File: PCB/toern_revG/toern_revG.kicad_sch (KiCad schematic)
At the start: 106 parts, among them IC1 BQ24075TRGTR, J1 AudioJack3_Switch, J10 Conn_01x02, J11 Conn_01x05, J11.5 Conn_01x05, J12 Conn_01x05, J13 Conn_01x05, J14 Conn_01x05, J15 Conn_01x05, J16 Conn_01x02, J17 AudioJack3_Ground, J18 Conn_01x05_Socket, J19 Conn_01x05_Socket, J2 Conn_01x05_Socket, J20 Conn_01x05_Socket, J21 Conn_01x05_Socket, J22 Conn_01x05_Socket, J23 Conn_01x05_Socket, J24 Conn_01x05_Socket, J3 AudioJack3_Ground, J4 USB_C_Receptacle_USB2.0, J5 AudioJack3_Switch, J6 AudioJack3_Switch, J7 AudioJack3_Switch, J8 Micro_SD_Card, J9 Conn_01x03, U1 SPX3819M5-L-3-3, U10 01x05 Connector_PinSocket_2.5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, U11 01x05 Connector_PinSocket_2.5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, U12 01x05 Connector_PinSocket_2.5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, U13 PAM8403D, U2 SPX3819M5-L-1-8, U3 SGTL5000XNBA3, U4 TLP2361V4_E, U5 74LVC2G14, U6 Teensy4.1, U7 SPX3819M5-L-3-3, U9 01x05 Connector_PinSocket_2.5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

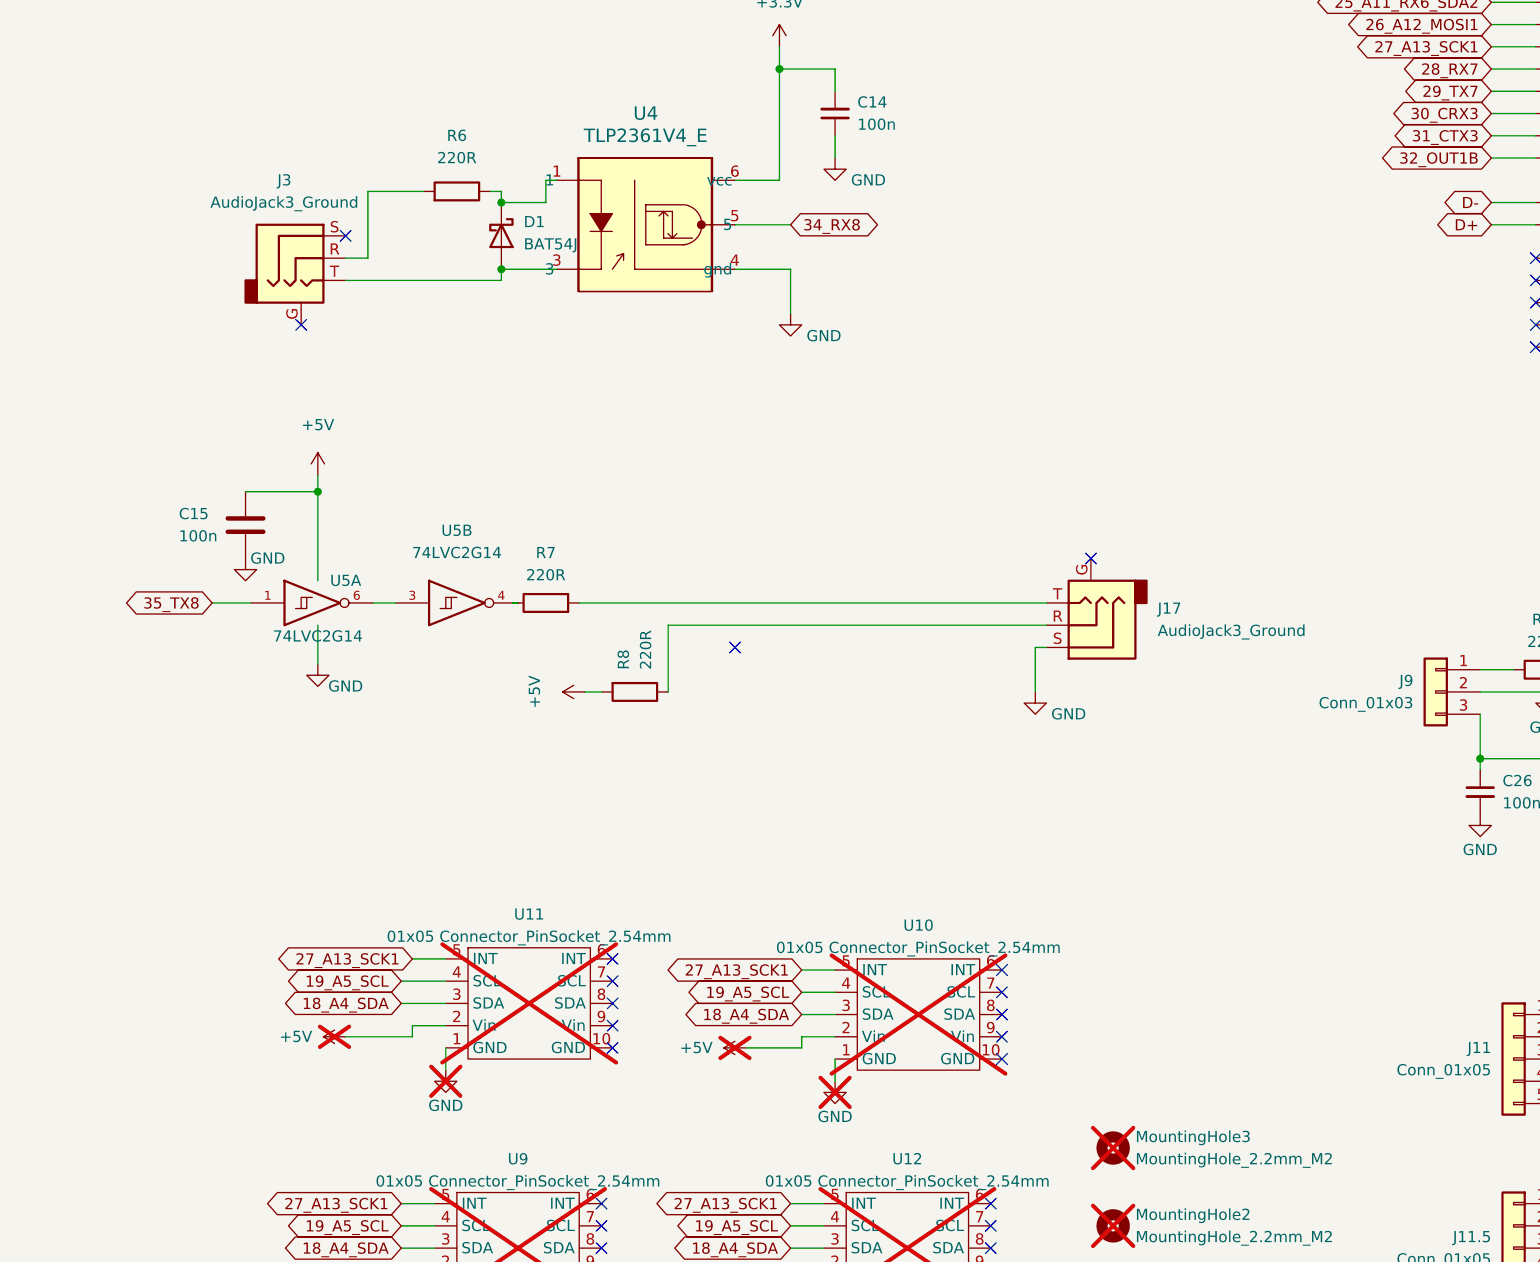
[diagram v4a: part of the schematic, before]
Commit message: better loading and saving speed and progress
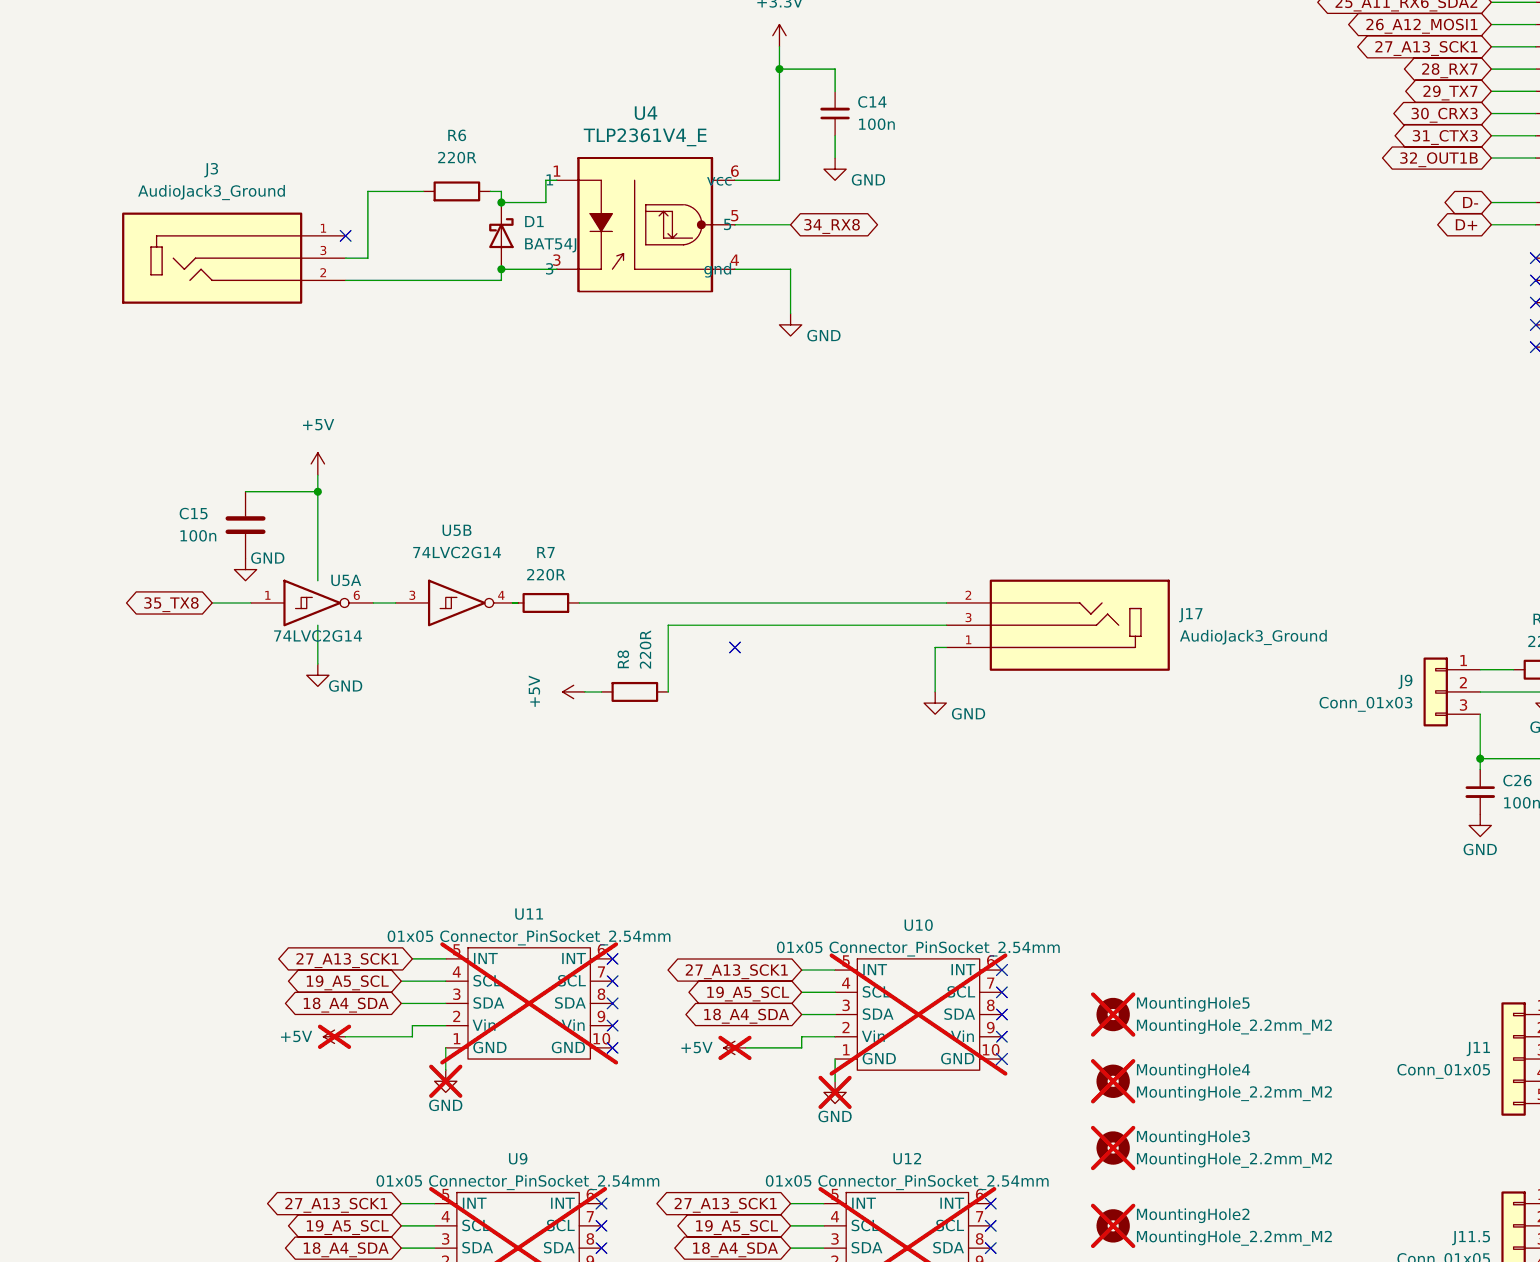
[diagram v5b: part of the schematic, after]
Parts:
- added MountingHole4, MountingHole5: MountingHole_2.2mm_M2, MountingHole:MountingHole_2.2mm_M2, symbol Mechanical:MountingHole
- IC1: footprint QFN50P300X300X100-17N-D -> BQ24075TRGTR:QFN50P300X300X100-17N-D
- J17, J3: footprint Connector_Audio:Jack_3.5mm_CUI_SJ1-3533NG_Horizontal_CircularHoles -> SJ1-3533:CUI_SJ1-3533; symbol Connector_Audio:AudioJack3_Ground -> SJ1-3533:SJ1-3533; Availability (none) -> In Stock; Check_prices (none) -> https://www.snapeda.com/parts/SJ1-3533/Same+Sky/view-part/?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; Description_1 (none) -> 3.5 mm Right-Angle Stereo Jack, 3 Pin PCB Mount, Threaded w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; LCSC C4992548 -> C4991776; MANUFACTURER (none) -> CUI Devices; MF (none) -> Same Sky; MP (none) -> SJ1-3533; PARTREV (none) -> 1.01; Package (none) -> None; Price (none) -> None; STANDARD (none) -> Manufacturer Recommendations; SnapEDA_Link (none) -> https://www.snapeda.com/parts/SJ1-3533/Same+Sky/view-part/?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; lcsc# C4992548 -> C4991776
- S1: footprint Button_Switch_THT:SW_E-Switch_EG2219_DPDT_Angled -> EG2219:EG2219
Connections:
- net GND: now also J17.1; no longer J17.S
- net at R7.2: now also J17.2; no longer J17.T
- net at R6.2: now also J3.3; no longer J3.R
- net at D1.2 (A), U4.3: now also J3.2; no longer J3.T
- net at R8.1: now also J17.3; no longer J17.R
- no-connect marks 64 -> 62

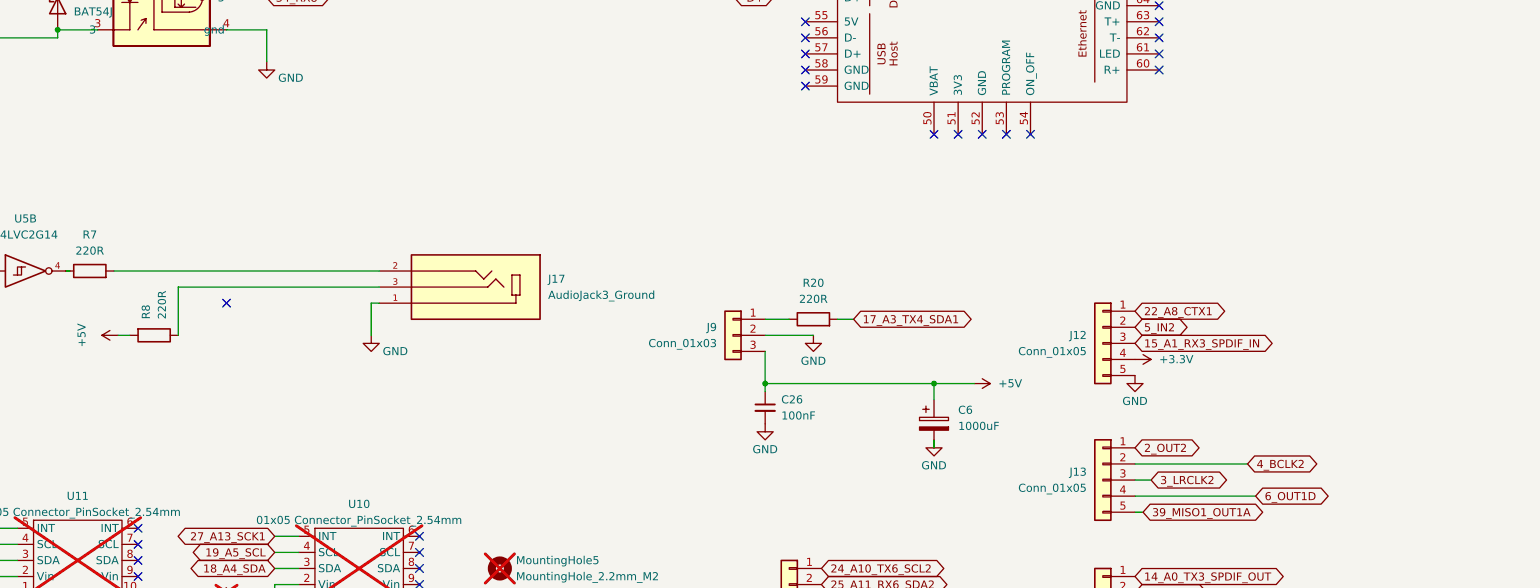
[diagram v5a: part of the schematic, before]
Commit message: small fixes in code, additional TPS22918DBVR for PCB (leds)
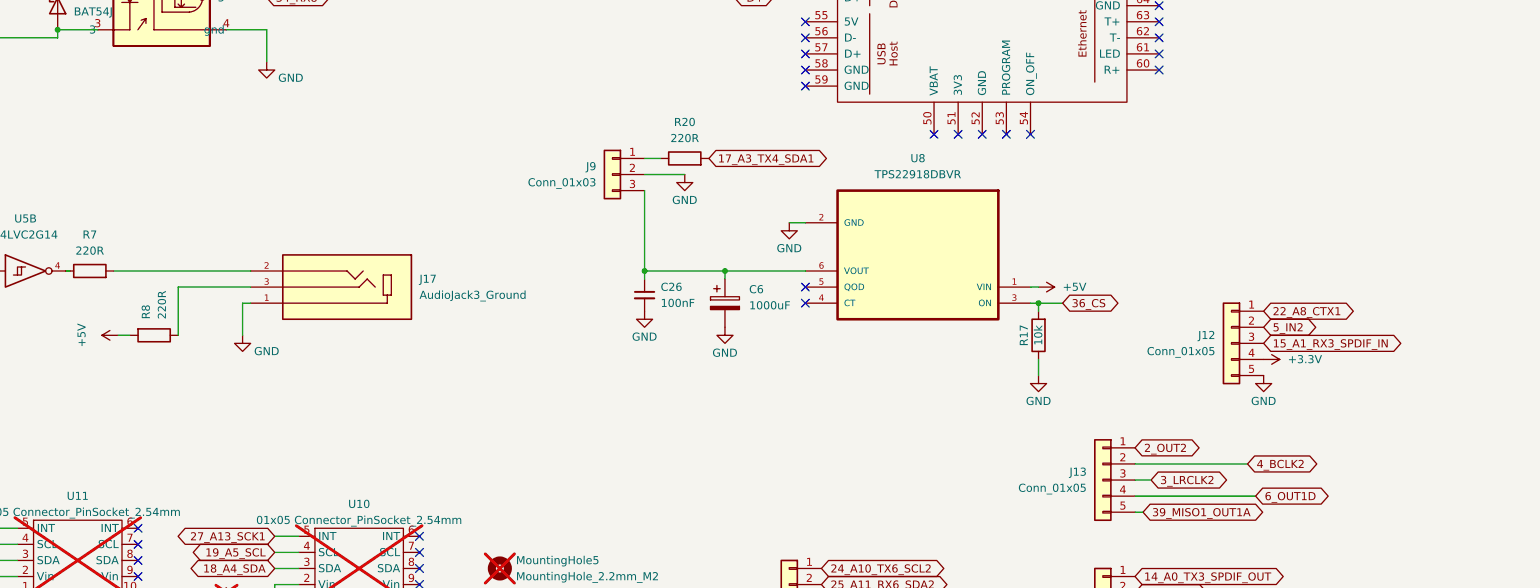
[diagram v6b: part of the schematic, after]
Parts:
- added R17: 10k, Resistor_SMD:R_0402_1005Metric, symbol Device:R
- added U8: TPS22918DBVR, TPS22918DBVR:SOT95P280X145-6N, symbol TPS22918DBVR:TPS22918DBVR
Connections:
- net +5V: now also U8.1 (VIN); no longer C26.1, C6.1, J9.3 (Pin_3)
- net 36_CS: now also R17.2, U8.3 (ON)
- net GND: now also R17.1, U8.2 (GND)
- new net: C26.1, C6.1, J9.3 (Pin_3), U8.6 (VOUT)
- no-connect marks 62 -> 63
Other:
- moved on the sheet: C26, C6, J12, J17, J9, R20

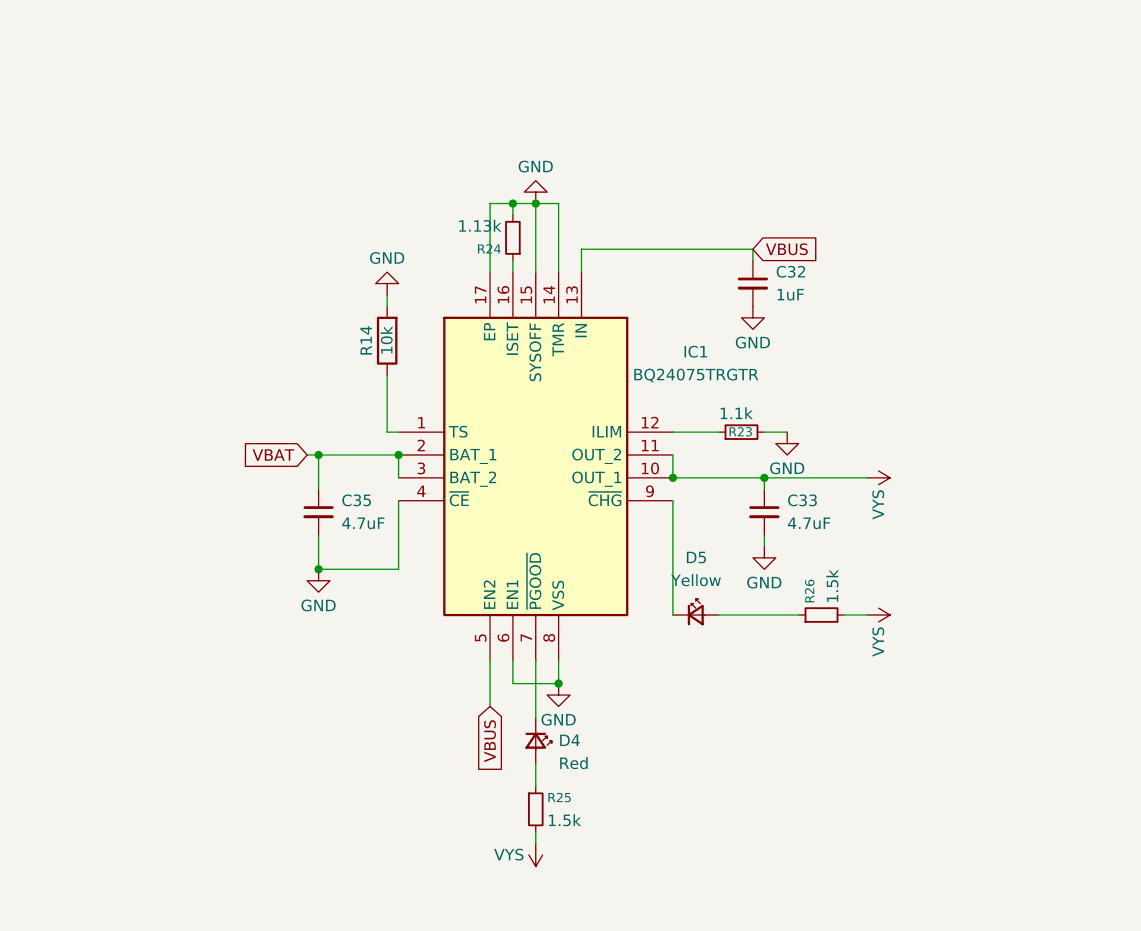
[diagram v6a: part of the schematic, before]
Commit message: fixed PCB: right resistors for TS + componentsize - final
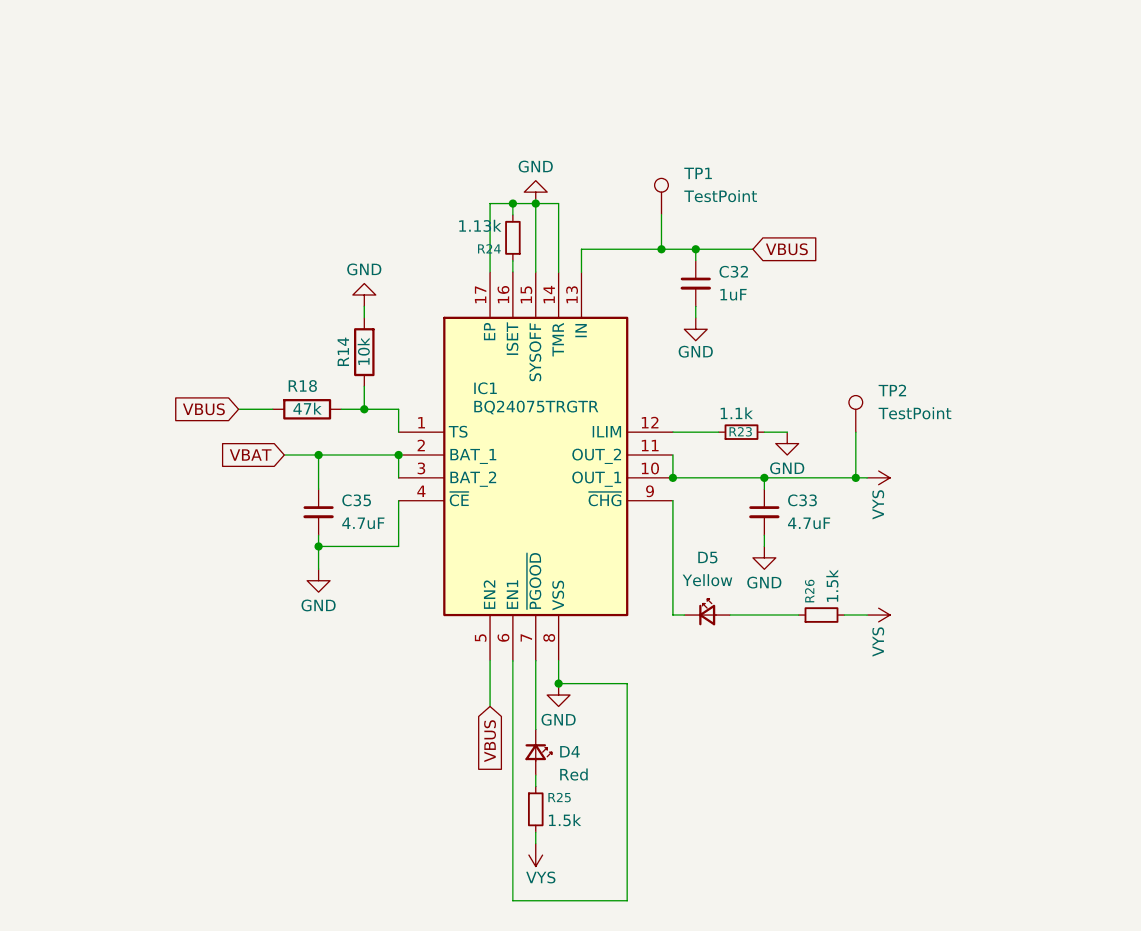
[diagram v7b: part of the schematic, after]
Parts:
- added R18: 47k, Resistor_SMD:R_0402_1005Metric, symbol Device:R
- added TP1, TP2: TestPoint, symbol Connector:TestPoint
- R24: lcsc# C67014 -> C166635; lscs# (none) -> C166635
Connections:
- net VBUS: now also R18.2, TP1.1
- net VYS: now also TP2.1
- net at IC1.1 (TS), R14.1: now also R18.1
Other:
- moved on the sheet: C32, D4, D5, R14
